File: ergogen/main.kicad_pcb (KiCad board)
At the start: 2 copper layers, 167.1 x 122.5 mm, 90 parts

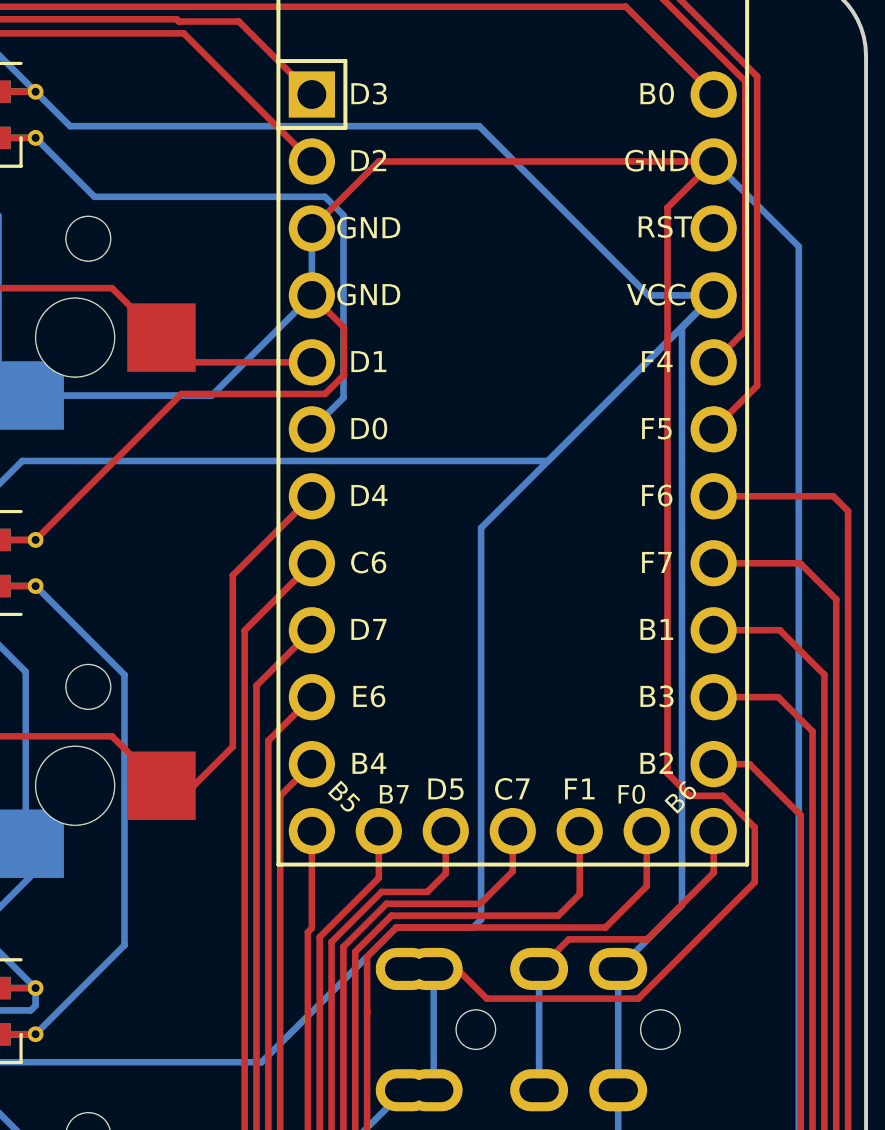
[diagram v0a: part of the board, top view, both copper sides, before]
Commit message: Fix TRRS pin in ergogen and kicad
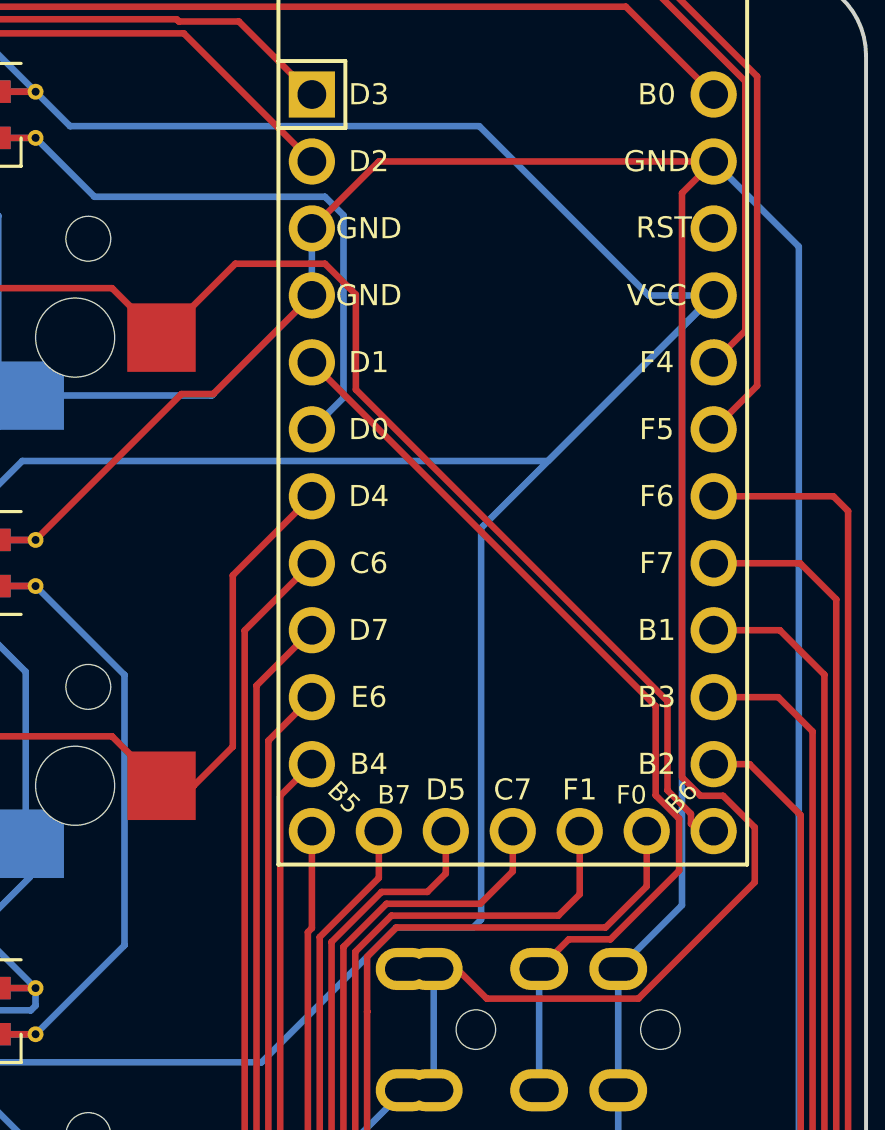
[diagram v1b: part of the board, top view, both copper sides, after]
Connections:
- REF** pad 1: D1 -> B6
- S18 pad 2: D1 -> B6
- TRRS1 pad 3: B6 -> D1
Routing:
- net B6: track 14.3 -> 55.3 mm
- net D1: track 24.8 -> 36.5 mm
- net GND: track 1241.2 -> 1237.0 mm
